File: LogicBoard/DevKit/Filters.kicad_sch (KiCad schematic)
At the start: 23 parts, among them U17 RS2057XH, U18 RS2057XH, U19 RS2057XH, U5 RS2057XH

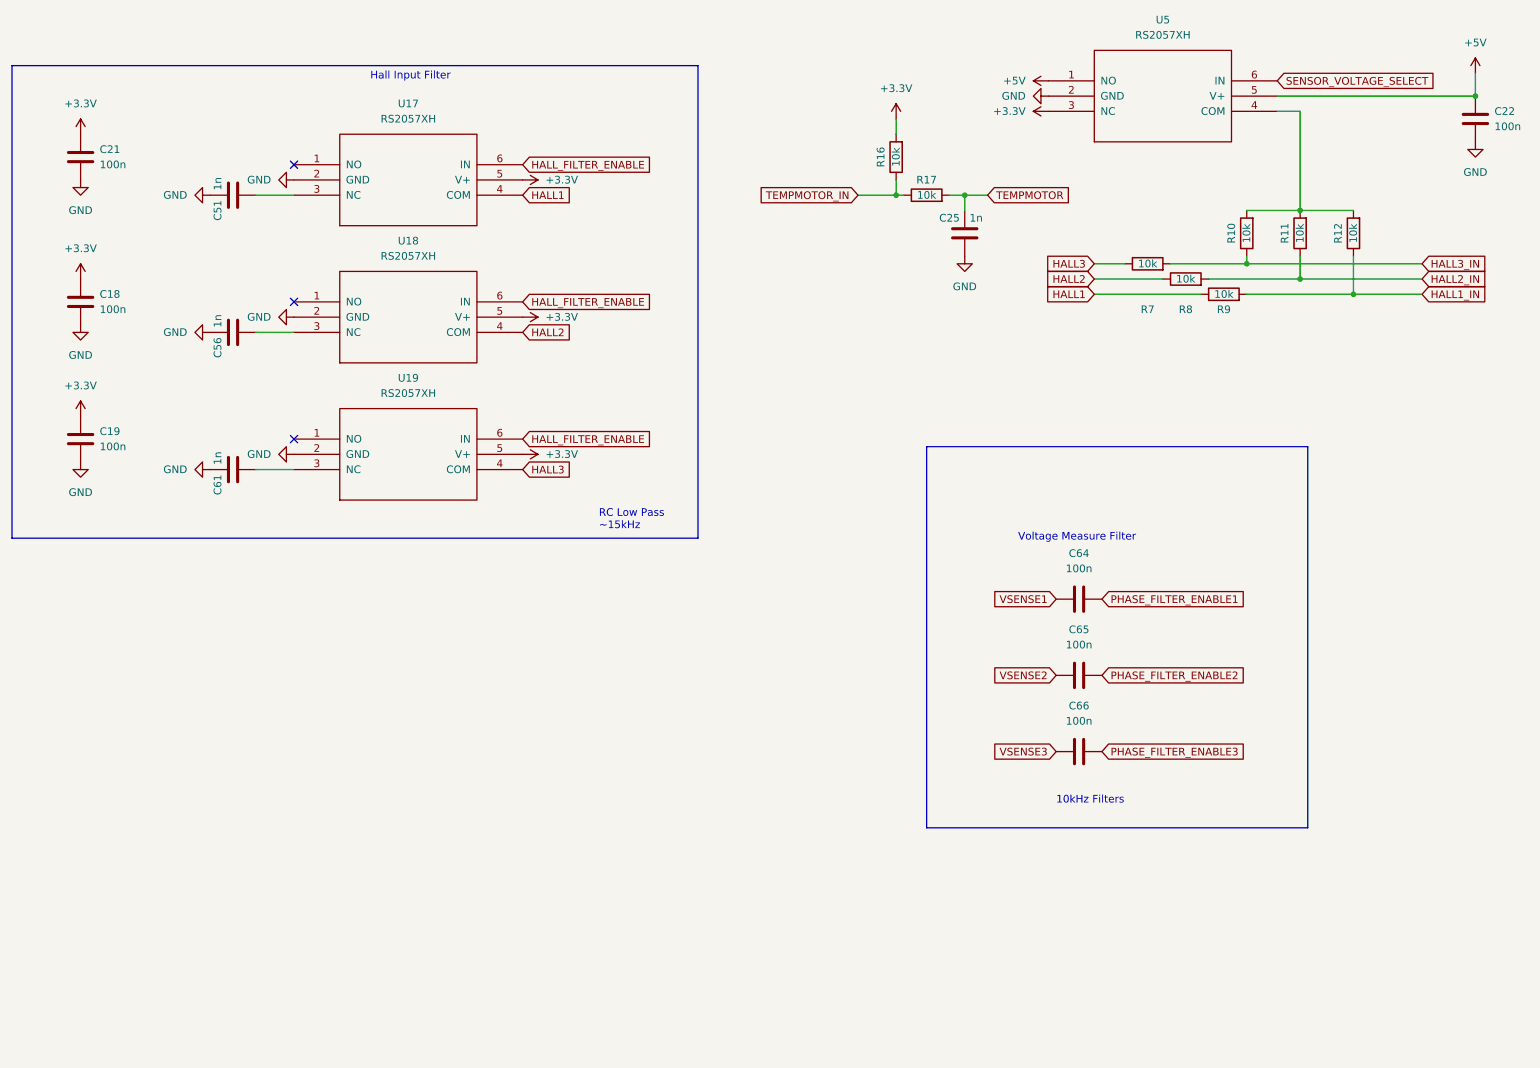
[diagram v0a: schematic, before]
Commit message: v3.3.2 - ECP2304 changes
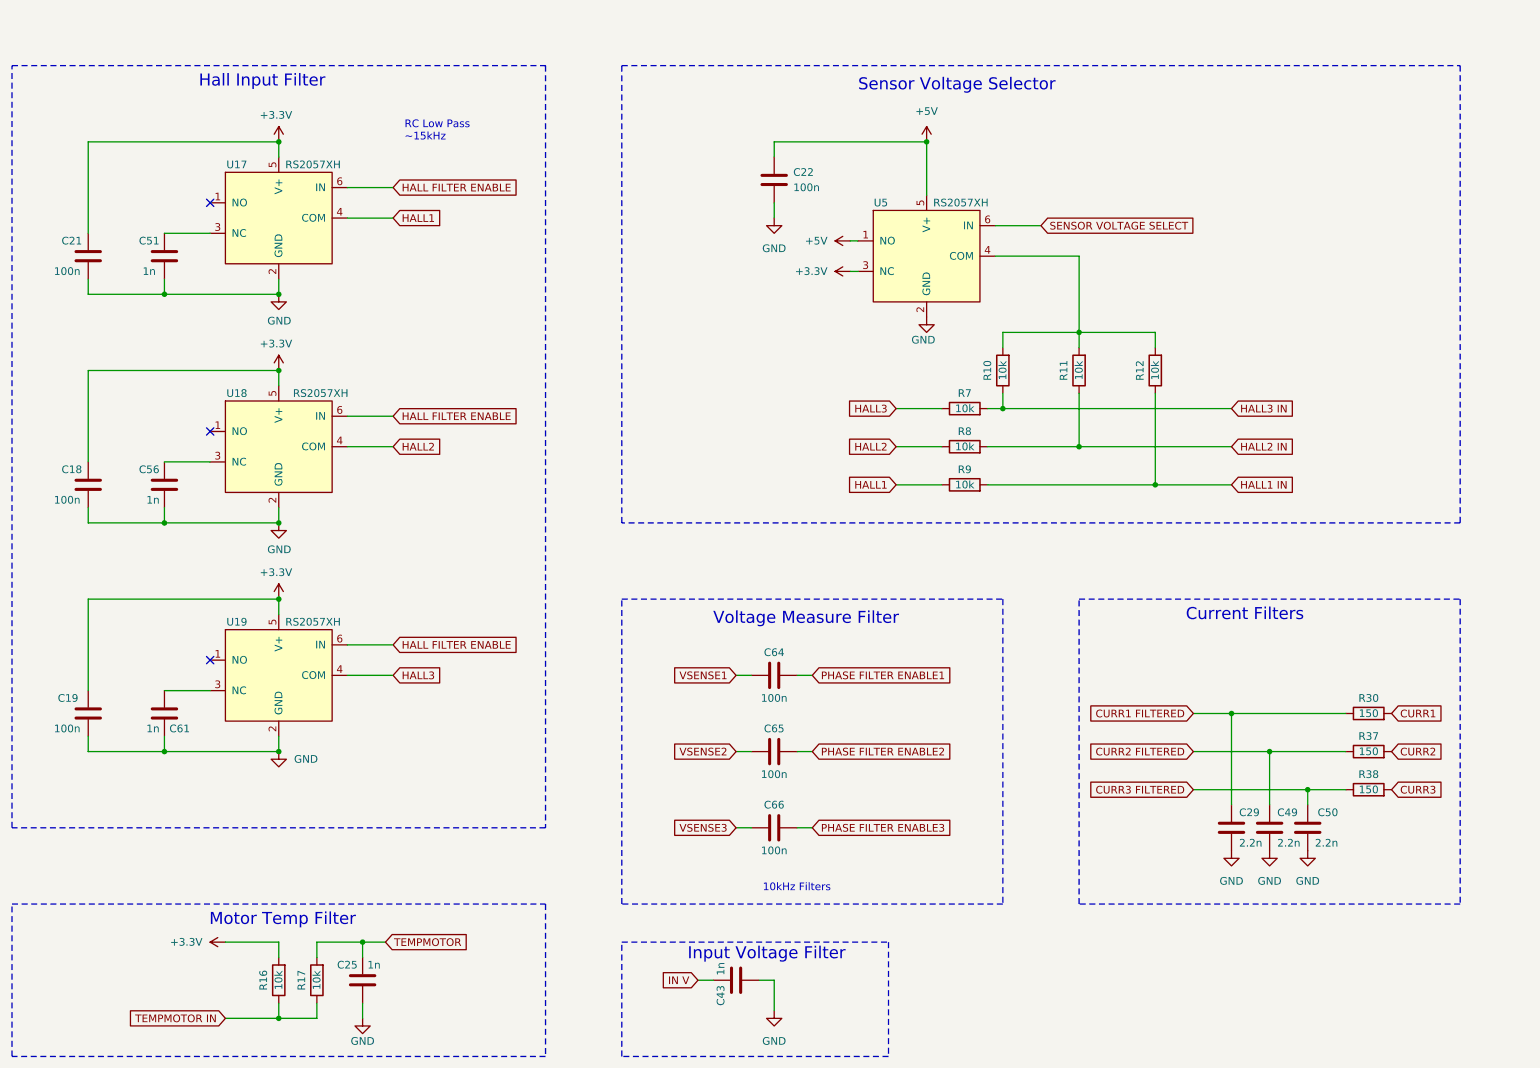
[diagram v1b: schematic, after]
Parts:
- added C29, C49, C50: 2.2n, GigaVescLibs:C_0603_1608Metric_L, symbol Device:C
- added C43: 1n, GigaVescLibs:C_0603_1608Metric_L, symbol Device:C
- added R30, R37, R38: 150, Resistor_SMD:R_0603_1608Metric, symbol Device:R
- U17, U18, U19, U5: JLCRotOffset -180 -> 0
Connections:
- net GND: now also C29.2, C43.2, C49.2, C50.1
- net HALL1_IN renamed HALL1 IN
- net HALL2_IN renamed HALL2 IN
- net HALL3_IN renamed HALL3 IN
- net HALL_FILTER_ENABLE renamed HALL FILTER ENABLE
- net PHASE_FILTER_ENABLE1 renamed PHASE FILTER ENABLE1
- net PHASE_FILTER_ENABLE2 renamed PHASE FILTER ENABLE2
- net PHASE_FILTER_ENABLE3 renamed PHASE FILTER ENABLE3
- net SENSOR_VOLTAGE_SELECT renamed SENSOR VOLTAGE SELECT
- net TEMPMOTOR_IN renamed TEMPMOTOR IN
- new net CURR1: R30.2
- new net CURR1 FILTERED: C29.1, R30.1
- new net CURR2: R37.2
- new net CURR2 FILTERED: C49.1, R37.1
- new net CURR3: R38.2
- new net CURR3 FILTERED: C50.2, R38.1
- new net IN V: C43.1
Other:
- note added: "Current Filters"
- note added: "Input Voltage Filter"
- note added: "Motor Temp Filter"
- note added: "Sensor Voltage Selector"
- moved on the sheet: C18, C19, C21, C22, C25, C51, C56, C61, C64, C65, C66, R10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
